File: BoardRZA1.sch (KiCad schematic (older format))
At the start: 158 parts, among them CON1 USB-MINI-B, CON2 USB-A-PCB, CON3 microSD, CON4 BARREL_JACK, J1 VGA, J2 SUPP32, K1 CONN_3, P1 CONN_5X2, P10 CONN_1, P11 CONN_1, P12 CONN_1, P13 CONN_1, P14 CONN_1, P15 CONN_1, P16 CONN_1, P17 CONN_1, P2 CONN_1, P3 CONN_1, P4 CONN_1, P5 CONN_1, P6 CONN_1, P7 CONN_1, P8 CONN_1, P9 CONN_1, SW1 RESET, SW2 NMI, SW3 SW0, SW4 SW1, U1 RZ-A1L, U2 13MHz, U3 48MHz, U4 N25QXXX, U5 AS4C16M16S, U6 BA3259HFP, U7 BU42xx, U8 TL074, X1 32.768k

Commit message: Update diagrams and pictures (1)
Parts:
- removed unit 1 of U8
- added unit 4 of U8
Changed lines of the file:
@@
 LIBS:vga
 LIBS:BoardRZA1-cache
-EELAYER 24 0
+EELAYER 25 0
 EELAYER END
 $Descr A0 46811 33110
@@
 L TL074 U8
 U 3 1 54F0D2A4
-P 9850 16200
-F 0 "U8" H 9900 16400 60  0000 C CNN
-F 1 "TL074" H 10000 16000 50  0000 C CNN
-F 2 "SMD_Packages:SO14E" H 9850 16200 60  0001 C CNN
-F 3 "" H 9850 16200 60  0000 C CNN
-	3    9850 16200
-	1    0    0    -1
-$EndComp
-$Comp
-L TL074 U8
-U 2 1 54F0F3D9
-P 9850 15200
-F 0 "U8" H 9900 15400 60  0000 C CNN
-F 1 "TL074" H 10000 15000 50  0000 C CNN
-F 2 "SMD_Packages:SO14E" H 9850 15200 60  0001 C CNN
-F 3 "" H 9850 15200 60  0000 C CNN
-	2    9850 15200
-	1    0    0    -1
-$EndComp
-$Comp
-L TL074 U8
-U 1 1 54F0FC73
 P 9850 14250
 F 0 "U8" H 9900 14450 60  0000 C CNN
@@
 F 2 "SMD_Packages:SO14E" H 9850 14250 60  0001 C CNN
 F 3 "" H 9850 14250 60  0000 C CNN
-	1    9850 14250
+	3    9850 14250
+	1    0    0    -1
+$EndComp
+$Comp
+L TL074 U8
+U 2 1 54F0F3D9
+P 9850 16200
+F 0 "U8" H 9900 16400 60  0000 C CNN
+F 1 "TL074" H 10000 16000 50  0000 C CNN
+F 2 "SMD_Packages:SO14E" H 9850 16200 60  0001 C CNN
+F 3 "" H 9850 16200 60  0000 C CNN
+	2    9850 16200
 	1    0    0    -1
 $EndComp
@@
 	-1   0    0    -1
 $EndComp
+$Comp
+L TL074 U8
+U 4 1 54FC8FBE
+P 9850 15200
+F 0 "U8" H 9900 15400 60  0000 C CNN
+F 1 "TL074" H 10000 15000 50  0000 C CNN
+F 2 "" H 9850 15200 60  0000 C CNN
+F 3 "" H 9850 15200 60  0000 C CNN
+	4    9850 15200
+	1    0    0    -1
+$EndComp
 $EndSCHEMATC

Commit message: Actualized schematic
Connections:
- net labels added: SYS_CLK
- wire segments 584 -> 583
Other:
- moved on the sheet: BSCANP1, C1, C10, C11, C12, C13, C14, C15, C16, C17, C18, C19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

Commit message: Change R2R DAC for ADV7125 on LQFP48
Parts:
- removed R22, R23: 10k, footprints:SM0805, symbol R
- removed RP1, RP2, RP3: 20k, Resistors_SMD:r_cat16-8, symbol R_PACK8
- removed RP4, RP5, RP6: 10k, Resistors_SMD:r_cat16-8, symbol R_PACK8
- removed U8: TL074, SMD_Packages:SO14E, symbol TL074
- added C54, C55, C56, C57, C58: 100n, footprints:SM0805, symbol Csmall
- added U8: ADV7125-lqfp48, Housings_QFP:lqfp-48, symbol ADV7125-lqfp48
- R21: value 10k -> 560R
- R24, R25, R26: value 280R -> 75R
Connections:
- net labels added: VGAB, VGAG, VGAR
- net labels removed: VGA_B, VGA_G, VGA_R
- wire segments 583 -> 487
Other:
- moved on the sheet: C34, C35, J1, J2, K1, P3, P4, R2, R24, R25, R26, R3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

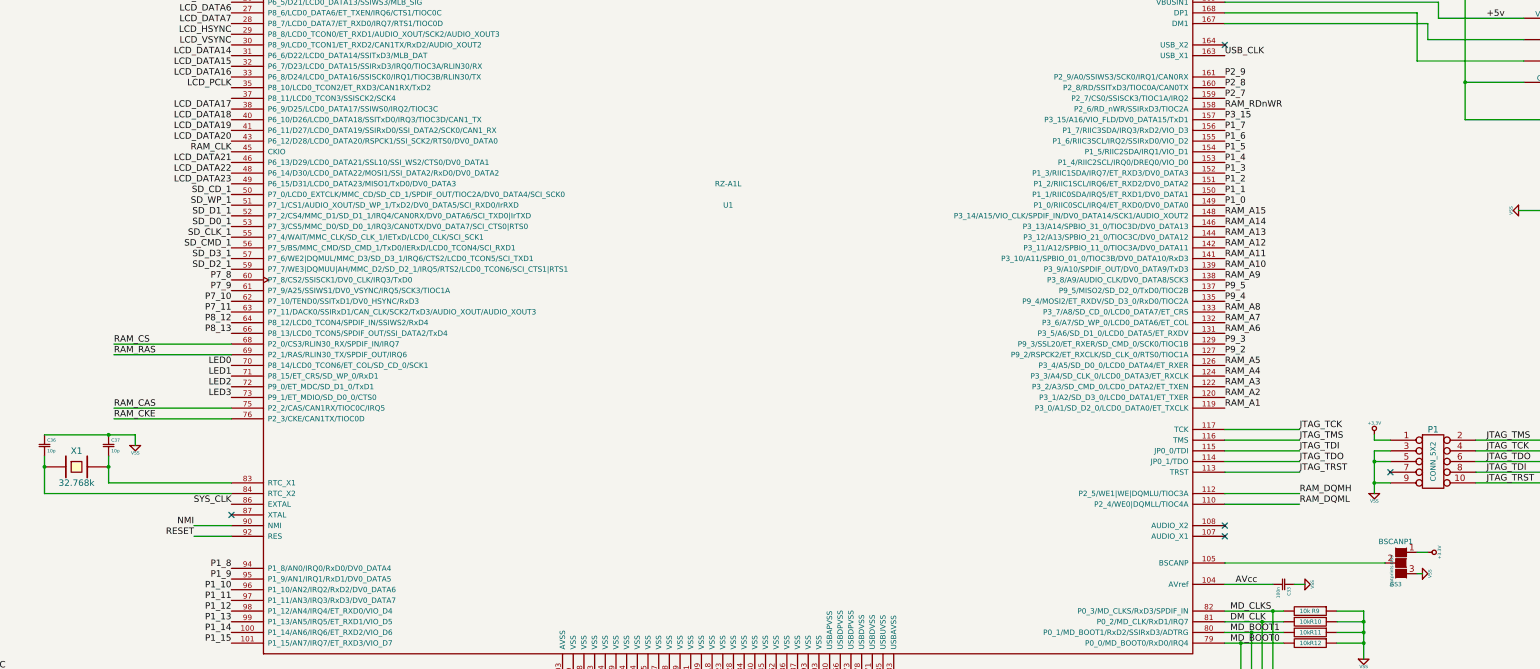
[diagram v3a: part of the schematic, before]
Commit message: Change SD_*_1 to SD_*_0 because LCD0_CLK is overlapped by SD_CLK_1
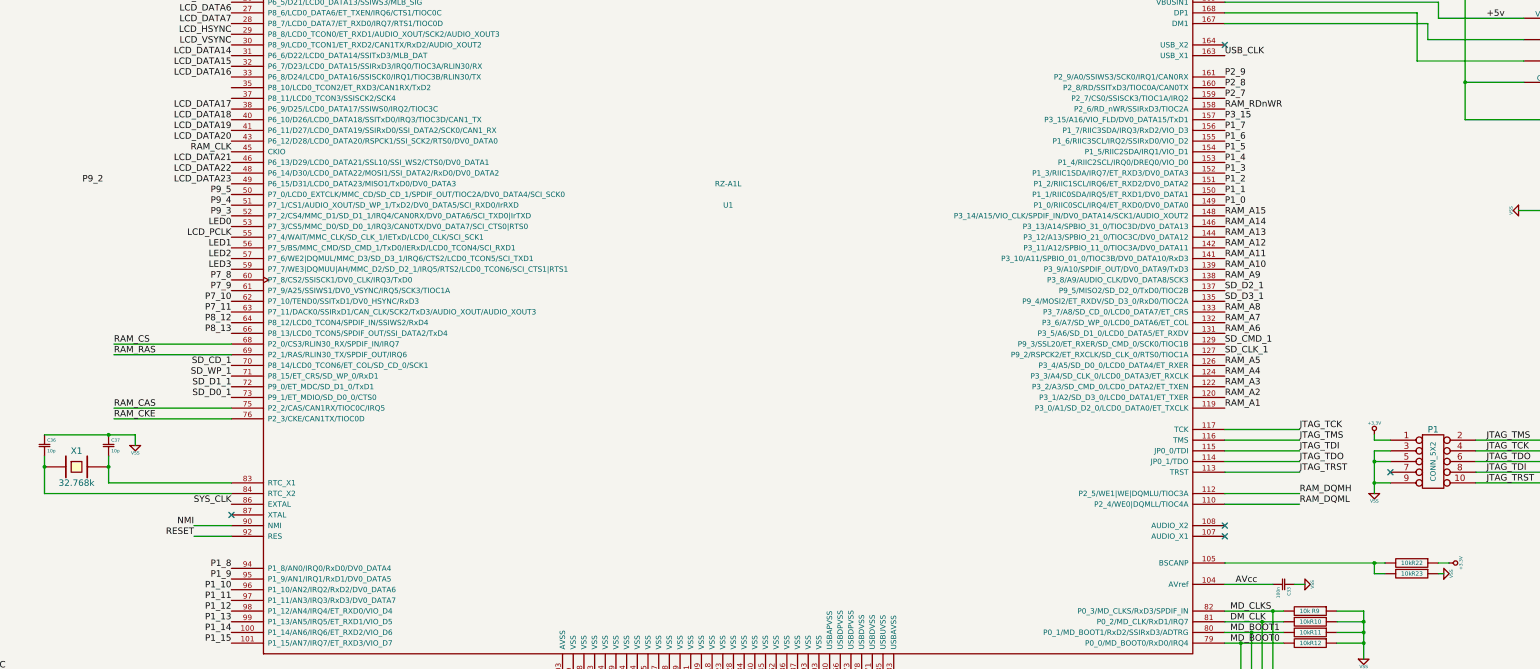
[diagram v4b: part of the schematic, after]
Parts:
- removed BSCANP1: GS3, footprints:GS3, symbol GS3
- added R22, R23: 10k, footprints:SM0805, symbol R
- U8: footprint Housings_QFP:lqfp-48 -> footprints:TQFP-48_Reflow
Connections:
- net +3.3V: now also R22.1
- net LCD_PCLK: now also U1.55 (P7_4/WAIT/MMC_CLK/SD_CLK_1/IETxD/LCD0_CLK/SCI_SCK1); no longer U1.35 (P8_10/LCD0_TCON2/ET_RXD3/CAN1RX/TxD2)
- net LED0: now also U1.53 (P7_3/CS5/MMC_D0/SD_D0_1/IRQ3/CAN0TX/DV0_DATA7/SCI_CTS0|RTS0); no longer U1.70 (P8_14/LCD0_TCON6/ET_COL/SD_CD_0/SCK1)
- net LED1: now also U1.56 (P7_5/BS/MMC_CMD/SD_CMD_1/TxD0/IERxD/LCD0_TCON4/SCI_RXD1); no longer U1.71 (P8_15/ET_CRS/SD_WP_0/RxD1)
- net LED2: now also U1.57 (P7_6/WE2|DQMUL/MMC_D3/SD_D3_1/IRQ6/CTS2/LCD0_TCON5/SCI_TXD1); no longer U1.72 (P9_0/ET_MDC/SD_D1_0/TxD1)
- net LED3: now also U1.59 (P7_7/WE3|DQMUU|AH/MMC_D2/SD_D2_1/IRQ5/RTS2/LCD0_TCON6/SCI_CTS1|RTS1); no longer U1.73 (P9_1/ET_MDIO/SD_D0_0/CTS0)
- net P9_2: no longer U1.127 (P9_2/RSPCK2/ET_RXCLK/SD_CLK_0/RTS0/TIOC1A)
- net P9_3: now also U1.52 (P7_2/CS4/MMC_D1/SD_D1_1/IRQ4/CAN0RX/DV0_DATA6/SCI_TXD0|IrTXD); no longer U1.129 (P9_3/SSL20/ET_RXER/SD_CMD_0/SCK0/TIOC1B)
- net P9_4: now also U1.51 (P7_1/CS1/AUDIO_XOUT/SD_WP_1/TxD2/DV0_DATA5/SCI_RXD0/IrRXD); no longer U1.135 (P9_4/MOSI2/ET_RXDV/SD_D3_0/RxD0/TIOC2A)
- net P9_5: now also U1.50 (P7_0/LCD0_EXTCLK/MMC_CD/SD_CD_1/SPDIF_OUT/TIOC2A/DV0_DATA4/SCI_SCK0); no longer U1.137 (P9_5/MISO2/SD_D2_0/TxD0/TIOC2B)
- net SD_CD_1: now also U1.70 (P8_14/LCD0_TCON6/ET_COL/SD_CD_0/SCK1); no longer U1.50 (P7_0/LCD0_EXTCLK/MMC_CD/SD_CD_1/SPDIF_OUT/TIOC2A/DV0_DATA4/SCI_SCK0)
- net SD_CLK_1: now also U1.127 (P9_2/RSPCK2/ET_RXCLK/SD_CLK_0/RTS0/TIOC1A); no longer U1.55 (P7_4/WAIT/MMC_CLK/SD_CLK_1/IETxD/LCD0_CLK/SCI_SCK1)
- net SD_CMD_1: now also U1.129 (P9_3/SSL20/ET_RXER/SD_CMD_0/SCK0/TIOC1B); no longer U1.56 (P7_5/BS/MMC_CMD/SD_CMD_1/TxD0/IERxD/LCD0_TCON4/SCI_RXD1)
- net SD_D0_1: now also U1.73 (P9_1/ET_MDIO/SD_D0_0/CTS0); no longer U1.53 (P7_3/CS5/MMC_D0/SD_D0_1/IRQ3/CAN0TX/DV0_DATA7/SCI_CTS0|RTS0)
- net SD_D1_1: now also U1.72 (P9_0/ET_MDC/SD_D1_0/TxD1); no longer U1.52 (P7_2/CS4/MMC_D1/SD_D1_1/IRQ4/CAN0RX/DV0_DATA6/SCI_TXD0|IrTXD)
- net SD_D2_1: now also U1.137 (P9_5/MISO2/SD_D2_0/TxD0/TIOC2B); no longer U1.59 (P7_7/WE3|DQMUU|AH/MMC_D2/SD_D2_1/IRQ5/RTS2/LCD0_TCON6/SCI_CTS1|RTS1)
- net SD_D3_1: now also U1.135 (P9_4/MOSI2/ET_RXDV/SD_D3_0/RxD0/TIOC2A); no longer U1.57 (P7_6/WE2|DQMUL/MMC_D3/SD_D3_1/IRQ6/CTS2/LCD0_TCON5/SCI_TXD1)
- net SD_WP_1: now also U1.71 (P8_15/ET_CRS/SD_WP_0/RxD1); no longer U1.51 (P7_1/CS1/AUDIO_XOUT/SD_WP_1/TxD2/DV0_DATA5/SCI_RXD0/IrRXD)
- net VSS: now also R23.1
- net at U1.105 (BSCANP): now also R22.2, R23.2
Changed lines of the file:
@@
 JTAG_TRST
 $Comp
-L GS3 BSCANP1
-U 1 1 5455B1D5
-P 19950 11250
-F 0 "BSCANP1" H 20000 11450 50  0000 C CNN
-F 1 "GS3" H 20000 11051 40  0000 C CNN
-F 2 "footprints:GS3" V 20038 11176 30  0000 C CNN
-F 3 "" H 19950 11250 60  0000 C CNN
-	1    19950 11250
-	-1   0    0    -1
-$EndComp
-$Comp
 L VSS #PWR022
 U 1 1 5455B55E
-P 20150 11350
-F 0 "#PWR022" H 20150 11350 30  0001 C CNN
-F 1 "VSS" H 20150 11280 30  0000 C CNN
-F 2 "" H 20150 11350 60  0000 C CNN
-F 3 "" H 20150 11350 60  0000 C CNN
-	1    20150 11350
+P 20350 11350
+F 0 "#PWR022" H 20350 11350 30  0001 C CNN
+F 1 "VSS" H 20350 11280 30  0000 C CNN
+F 2 "" H 20350 11350 60  0000 C CNN
+F 3 "" H 20350 11350 60  0000 C CNN
+	1    20350 11350
 	0    -1   -1   0
 $EndComp
@@
 L +3.3V #PWR023
 U 1 1 5455BCB5
-P 20200 11150
-F 0 "#PWR023" H 20200 11110 30  0001 C CNN
-F 1 "+3.3V" H 20200 11260 30  0000 C CNN
-F 2 "" H 20200 11150 60  0000 C CNN
-F 3 "" H 20200 11150 60  0000 C CNN
-	1    20200 11150
+P 20400 11250
+F 0 "#PWR023" H 20400 11210 30  0001 C CNN
+F 1 "+3.3V" H 20400 11360 30  0000 C CNN
+F 2 "" H 20400 11250 60  0000 C CNN
+F 3 "" H 20400 11250 60  0000 C CNN
+	1    20400 11250
 	0    1    1    0
 $EndComp
@@
 Text Label 3350 5100 0    60   ~ 0
 RAM_CLK
-Text Label 9000 7800 2    60   ~ 0
+Text Label 9000 9400 2    60   ~ 0
 SD_CD_1
-Text Label 9000 7900 2    60   ~ 0
+Text Label 9000 9500 2    60   ~ 0
 SD_WP_1
-Text Label 9000 8000 2    60   ~ 0
+Text Label 9000 9600 2    60   ~ 0
 SD_D1_1
-Text Label 9000 8100 2    60   ~ 0
+Text Label 9000 9700 2    60   ~ 0
 SD_D0_1
-Text Label 9000 8200 2    60   ~ 0
+Text Label 18300 9300 0    60   ~ 0
 SD_CLK_1
-Text Label 9000 8300 2    60   ~ 0
+Text Label 18300 9200 0    60   ~ 0
 SD_CMD_1
-Text Label 9000 8400 2    60   ~ 0
+Text Label 18300 8800 0    60   ~ 0
 SD_D3_1
-Text Label 9000 8500 2    60   ~ 0
+Text Label 18300 8700 0    60   ~ 0
 SD_D2_1
 Text Label 19500 2800 2    60   ~ 0
@@
 Text Label 1700 7750 2    60   ~ 0
 P7_11
-Text Label 9000 9400 2    60   ~ 0
+Text Label 9000 8100 2    60   ~ 0
 LED0
-Text Label 9000 9500 2    60   ~ 0
+Text Label 9000 8300 2    60   ~ 0
 LED1
-Text Label 9000 9600 2    60   ~ 0
+Text Label 9000 8400 2    60   ~ 0
 LED2
-Text Label 9000 9700 2    60   ~ 0
+Text Label 9000 8500 2    60   ~ 0
 LED3
 Text Label 18300 5200 0    60   ~ 0
@@
 Text Label 9000 6400 2    60   ~ 0
 LCD_VSYNC
-Text Label 9000 6800 2    60   ~ 0
+Text Label 9000 8200 2    60   ~ 0
 LCD_PCLK
 Text Label 6400 12450 0    60   ~ 0
@@
 	1    0    0    -1
 $EndComp
-Text Label 18300 9300 0    60   ~ 0
-P9_2
-Text Label 18300 9200 0    60   ~ 0
+Text Label 9000 8000 2    60   ~ 0
 P9_3
-Text Label 18300 8800 0    60   ~ 0
+Text Label 9000 7900 2    60   ~ 0
 P9_4
-Text Label 18300 8700 0    60   ~ 0
+Text Label 9000 7800 2    60   ~ 0
 P9_5
 Text Label 1700 8850 2    60   ~ 0
@@
 Connection ~ 7850 10050
 Wire Wire Line
-	20150 11350 20100 11350
+	20350 11350 20300 11350
 Wire Wire Line
-	20200 11150 20100 11150
+	20400 11250 20300 11250
 Wire Wire Line
 	6650 3300 6450 3300
@@
 F 0 "U8" H 2650 13050 50  0000 C CNN
 F 1 "ADV7125-lqfp48" H 2650 13250 50  0000 C CNN
-F 2 "Housings_QFP:lqfp-48" H 2650 13150 50  0001 C CNN
+F 2 "footprints:TQFP-48_Reflow" H 2650 13150 50  0001 C CNN
 F 3 "DOCUMENTATION" H 2650 13150 50  0001 C CNN
 	1    2650 13150
@@
 Wire Wire Line
 	1150 14600 1400 14600
+$Comp
+L R R22
+U 1 1 551EA37C
+P 20050 11250
+F 0 "R22" V 20050 11300 40  0000 C CNN
+F 1 "10k" V 20050 11200 40  0000 C CNN
+F 2 "footprints:SM0805" V 19980 11250 30  0001 C CNN
+F 3 "" H 20050 11250 30  0000 C CNN
+	1    20050 11250
+	0    1    1    0
+$EndComp
+$Comp
+L R R23
+U 1 1 551EA382
+P 20050 11350
+F 0 "R23" V 20050 11400 40  0000 C CNN
+F 1 "10k" V 20050 11300 40  0000 C CNN
+F 2 "footprints:SM0805" V 19980 11350 30  0001 C CNN
+F 3 "" H 20050 11350 30  0000 C CNN
+	1    20050 11350
+	0    1    1    0
+$EndComp
+Wire Wire Line
+	19800 11350 19700 11350
+Wire Wire Line
+	19700 11350 19700 11250
+Connection ~ 19700 11250
+Text Label 7800 7700 2    60   ~ 0
+P9_2
 $EndSCHEMATC

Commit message: Move VGA connector, MicroSD connector, reasign GPIO
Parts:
- added D8: LED, footprints:LED-0805, symbol LED
- added R27: 1k, footprints:SM0805, symbol R
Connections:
- net P9_2 is gone; now on net P1_12: J2.17
- net +3.3V: now also D8.2 (K)
- net LED0: now also U1.35 (P8_10/LCD0_TCON2/ET_RXD3/CAN1RX/TxD2); no longer U1.53 (P7_3/CS5/MMC_D0/SD_D0_1/IRQ3/CAN0TX/DV0_DATA7/SCI_CTS0|RTS0)
- net LED1: now also U1.37 (P8_11/LCD0_TCON3/SSISCK2/SCK4); no longer U1.56 (P7_5/BS/MMC_CMD/SD_CMD_1/TxD0/IERxD/LCD0_TCON4/SCI_RXD1)
- net LED2: now also U1.50 (P7_0/LCD0_EXTCLK/MMC_CD/SD_CD_1/SPDIF_OUT/TIOC2A/DV0_DATA4/SCI_SCK0); no longer U1.57 (P7_6/WE2|DQMUL/MMC_D3/SD_D3_1/IRQ6/CTS2/LCD0_TCON5/SCI_TXD1)
- net LED3: now also U1.51 (P7_1/CS1/AUDIO_XOUT/SD_WP_1/TxD2/DV0_DATA5/SCI_RXD0/IrRXD); no longer U1.59 (P7_7/WE3|DQMUU|AH/MMC_D2/SD_D2_1/IRQ5/RTS2/LCD0_TCON6/SCI_CTS1|RTS1)
- net P1_10: now also J2.19; no longer J2.23
- net P1_11: now also J2.18; no longer J2.22
- net P1_12: no longer J2.21
- net P1_13: now also J2.16; no longer J2.20
- net P1_14: now also J2.15; no longer J2.19
- net P1_15: now also J2.14; no longer J2.18
- net P1_8: now also J2.21; no longer J2.25
- net P1_9: now also J2.20; no longer J2.24
- net P7_10: now also J2.25; no longer J2.29
- net P7_11: now also J2.24; no longer J2.28
- net P7_8: now also J2.27; no longer J2.31
- net P7_9: now also J2.26; no longer J2.30
- net P8_12 renamed P8_12(RXD)
- net P8_12(RXD): now also J2.23; no longer J2.27
- net P8_13 renamed P8_13(TXD)
- net P8_13(TXD): now also J2.22; no longer J2.26
- net P9_3 renamed LED4
- net LED4: now also R27.1; no longer J2.16
- removed net P9_4: J2.15, U1.51 (P7_1/CS1/AUDIO_XOUT/SD_WP_1/TxD2/DV0_DATA5/SCI_RXD0/IrRXD)
- removed net P9_5: J2.14, U1.50 (P7_0/LCD0_EXTCLK/MMC_CD/SD_CD_1/SPDIF_OUT/TIOC2A/DV0_DATA4/SCI_SCK0)
- new net: D8.1 (A), R27.2
- new net P7_3: J2.31, U1.53 (P7_3/CS5/MMC_D0/SD_D0_1/IRQ3/CAN0TX/DV0_DATA7/SCI_CTS0|RTS0)
- new net P7_5: J2.30, U1.56 (P7_5/BS/MMC_CMD/SD_CMD_1/TxD0/IERxD/LCD0_TCON4/SCI_RXD1)
- new net P7_6: J2.29, U1.57 (P7_6/WE2|DQMUL/MMC_D3/SD_D3_1/IRQ6/CTS2/LCD0_TCON5/SCI_TXD1)
- new net P7_7: J2.28, U1.59 (P7_7/WE3|DQMUU|AH/MMC_D2/SD_D2_1/IRQ5/RTS2/LCD0_TCON6/SCI_CTS1|RTS1)
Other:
- moved on the sheet: D1, D2, D3, D4, R45, R46, R47, R48

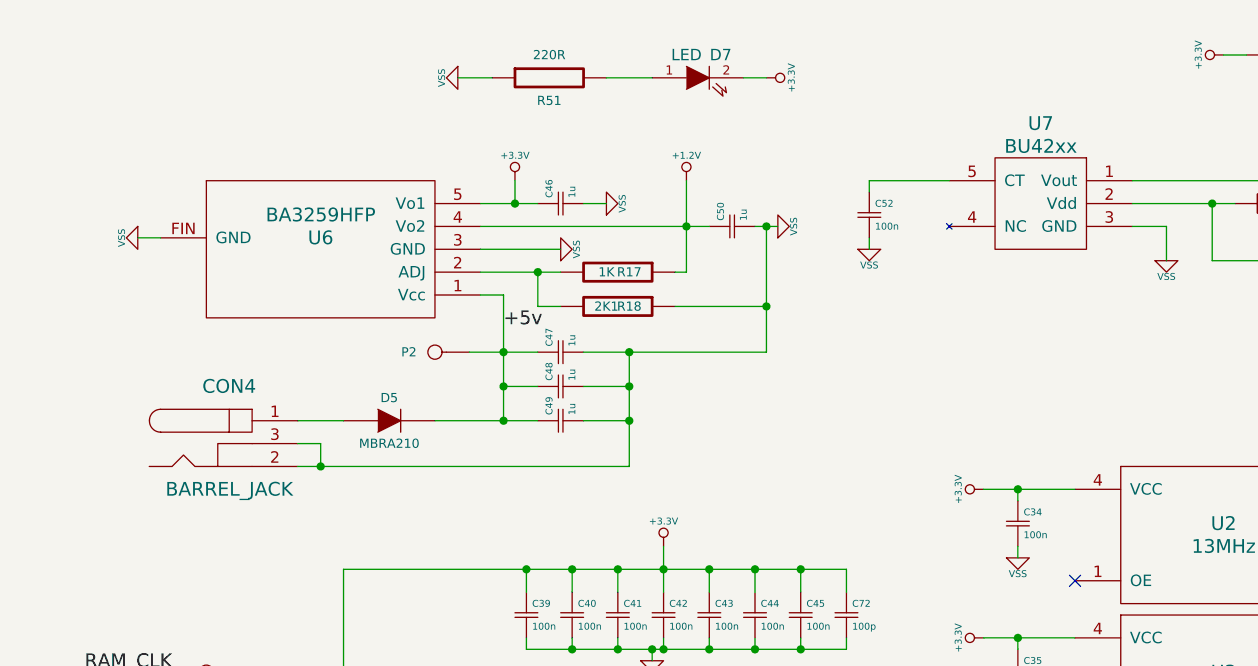
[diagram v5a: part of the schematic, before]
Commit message: Replace monlitic dual regulator by two XX1117-Y.Z
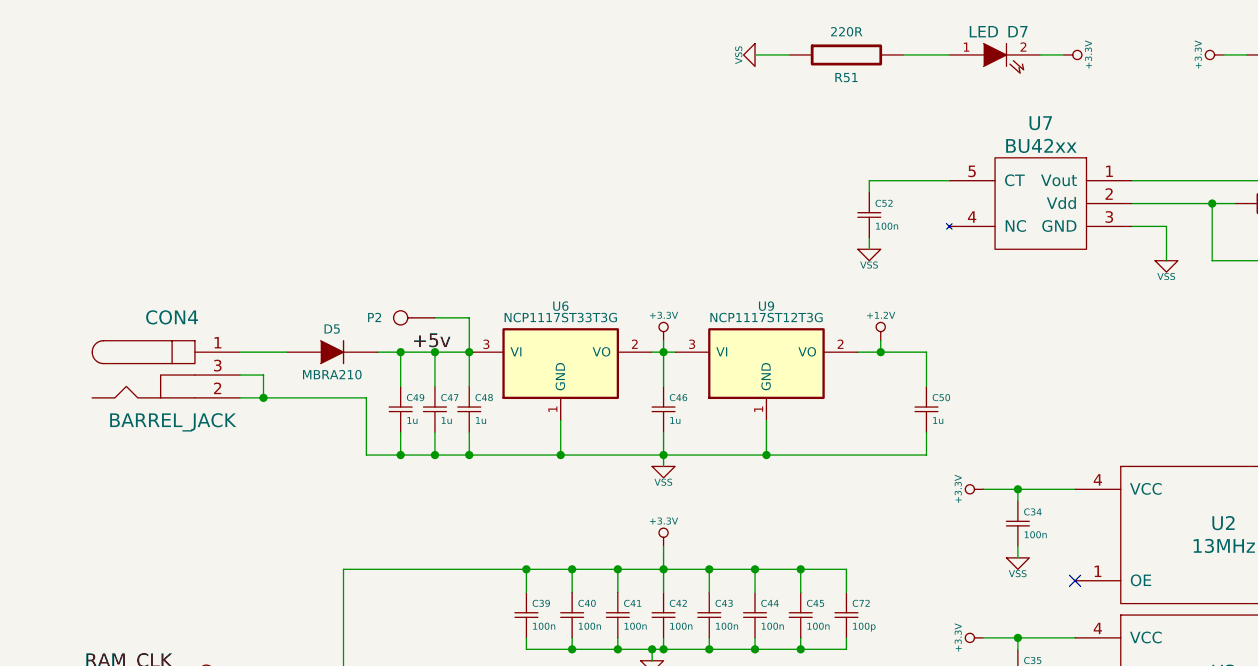
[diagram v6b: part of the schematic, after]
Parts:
- removed R17: 1K, footprints:SM0805, symbol R
- removed R18: 2K1, footprints:SM0805, symbol R
- removed U6: BA3259HFP, footprints:Rohm-HRP5, symbol BA3259HFP
- added U6: NCP1117ST33T3G, w_smd_trans.pretty:sot223, symbol NCP1117ST33T3G
- added U9: NCP1117ST12T3G, w_smd_trans.pretty:sot223, symbol NCP1117ST12T3G
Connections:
- net +1.2V: now also U9.2 (VO)
- net +3.3V: now also U6.2 (VO), U9.3 (VI)
- net +5v: now also U6.3 (VI)
- net VSS: now also U6.1 (GND), U9.1 (GND)
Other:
- moved on the sheet: C46, C47, C48, C49, C50, CON4, D5, D7, P2, R51

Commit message: New Routing
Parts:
- removed C10, C12, C20, C22, C27, C9: 100n, footprints:SM0805, symbol Csmall
- removed C47, C49: 1u, footprints:c_0805, symbol Csmall
- removed R11, R14, R15, R16: 10k, footprints:SM0805, symbol R
- C1, C11, C13, C14, C15, C16, C17, C18, C19, C2, C21, C23, C24, C25, C26, C28, C29, C3, C30, C31, C32, C33, C34, C35, C36, C37, C38, C39, C4, C40, C41, C42, C43, C44, C45, C46, C5, C52, C53, C54, C55, C56, C57, C58, C6, C67, C68, C69, C7, C70, C71, C72, C73, C74, C75, C76, C8: footprint footprints:SM0805 -> Capacitors_SMD:C_0805
- C48: value 1u -> 10u; footprint footprints:c_0805 -> Capacitors_SMD:C_0805
- C50, C51: footprint footprints:c_0805 -> Capacitors_SMD:C_0805
- R1, R10, R12, R19, R2, R20, R21, R22, R23, R24, R25, R26, R27, R3, R4, R42, R43, R44, R45, R46, R47, R48, R5, R50, R51, R6, R7, R8, R9: footprint footprints:SM0805 -> Resistors_SMD:R_0805
- R11: renamed from R13; footprint footprints:SM0805 -> Resistors_SMD:R_0805
- U8: footprint footprints:TQFP-48_Reflow -> w_smd_lqfp:lqfp48
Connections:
- net MD_BOOT1: now also R11.2
- net MD_CLKS: no longer R11.2
- net H_D-: now reaches CON2.2 (D-), U1.167 (DM1)
- net H_D+: now reaches CON2.3 (D+), U1.168 (DP1)
- net D_D-: now reaches CON1.2 (D-), U1.174 (DM0)
- net D_D+: now reaches CON1.3 (D+), U1.175 (DP0)
- net VBUS: now reaches CON1.1 (VBUS), D6.1 (A), U1.176 (VBUSIN0)
- net DCIN: now reaches CON4.1, D5.1 (A)
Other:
- moved on the sheet: R11
